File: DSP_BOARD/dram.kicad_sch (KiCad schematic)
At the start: 1 part, among them U2 Tz170J361

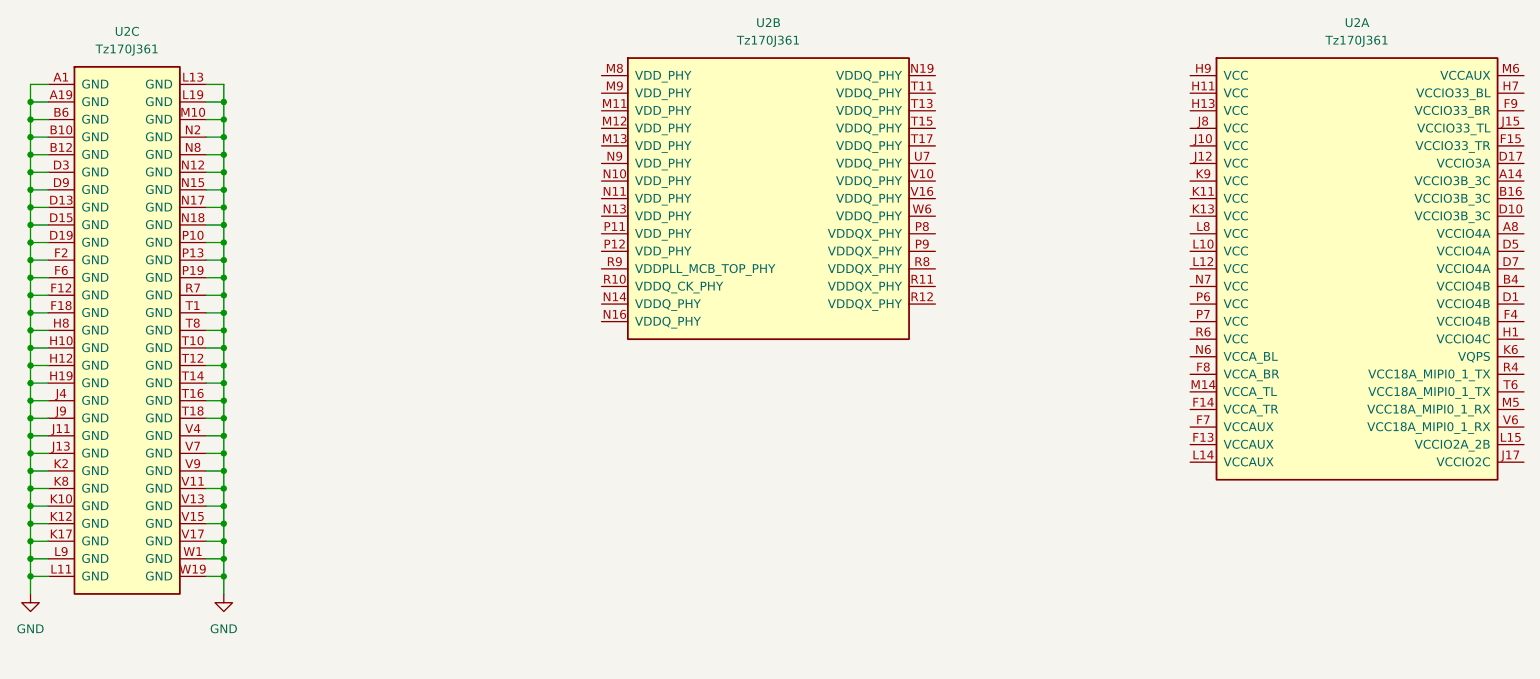
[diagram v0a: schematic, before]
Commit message: somewhat started on the DSP board, added in ADC, DAC and Tz170 symbols and footprints
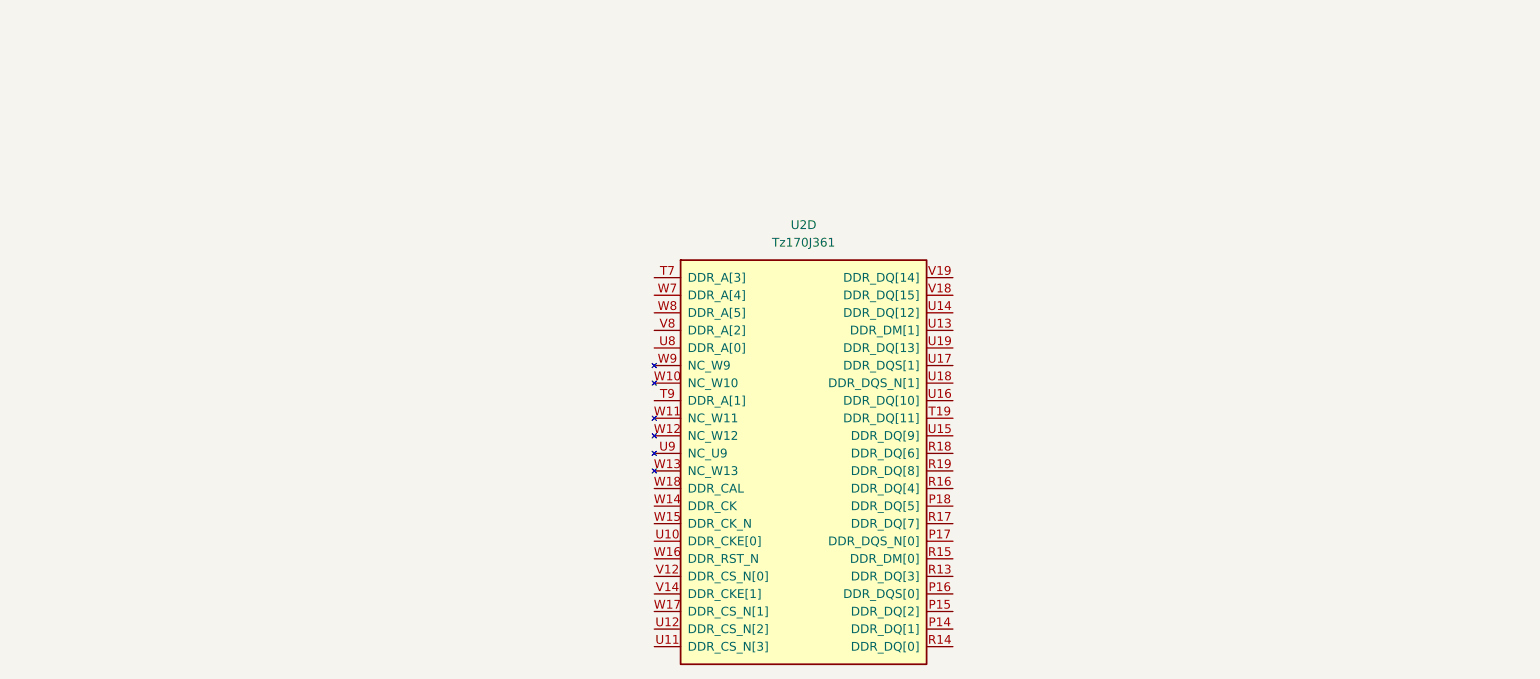
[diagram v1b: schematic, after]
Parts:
- removed U2: Tz170J361, Efinix:Efinix_FBGA-361_13x13mm_P0.65mm, symbol Efinix:Tz170J361
- added U2: Tz170J361, Efinix:Efinix_FBGA-361_13x13mm_P0.65mm, symbol Efinix:Tz170J361
